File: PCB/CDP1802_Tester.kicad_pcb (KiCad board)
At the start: 2 copper layers, 102.2 x 53.8 mm, 7 parts, among them SW1 SW_Push, SW2 SW_Push, SW3 SW_Push, SW4 SW_Push, SW5 SW_Push, U1 CDP1802ACE

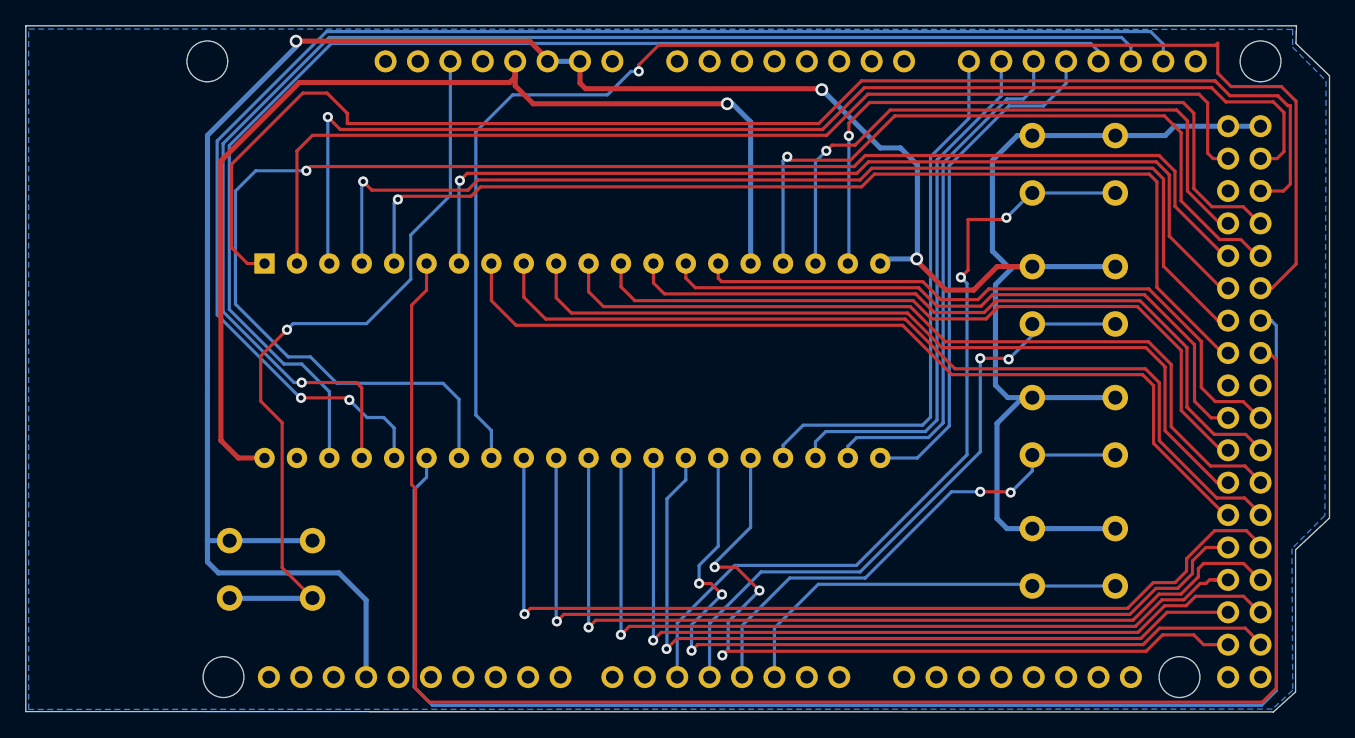
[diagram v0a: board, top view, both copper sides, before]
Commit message: Changed ZIF socket to wide (oval) pins Added jumper for pin 16 to either Vcc or A15 on the Arduino Added Reset button Set A15/PIN16 to OUTPUT and default HIGH Updated code to use SW3 to toggle the value of A15/PIN16
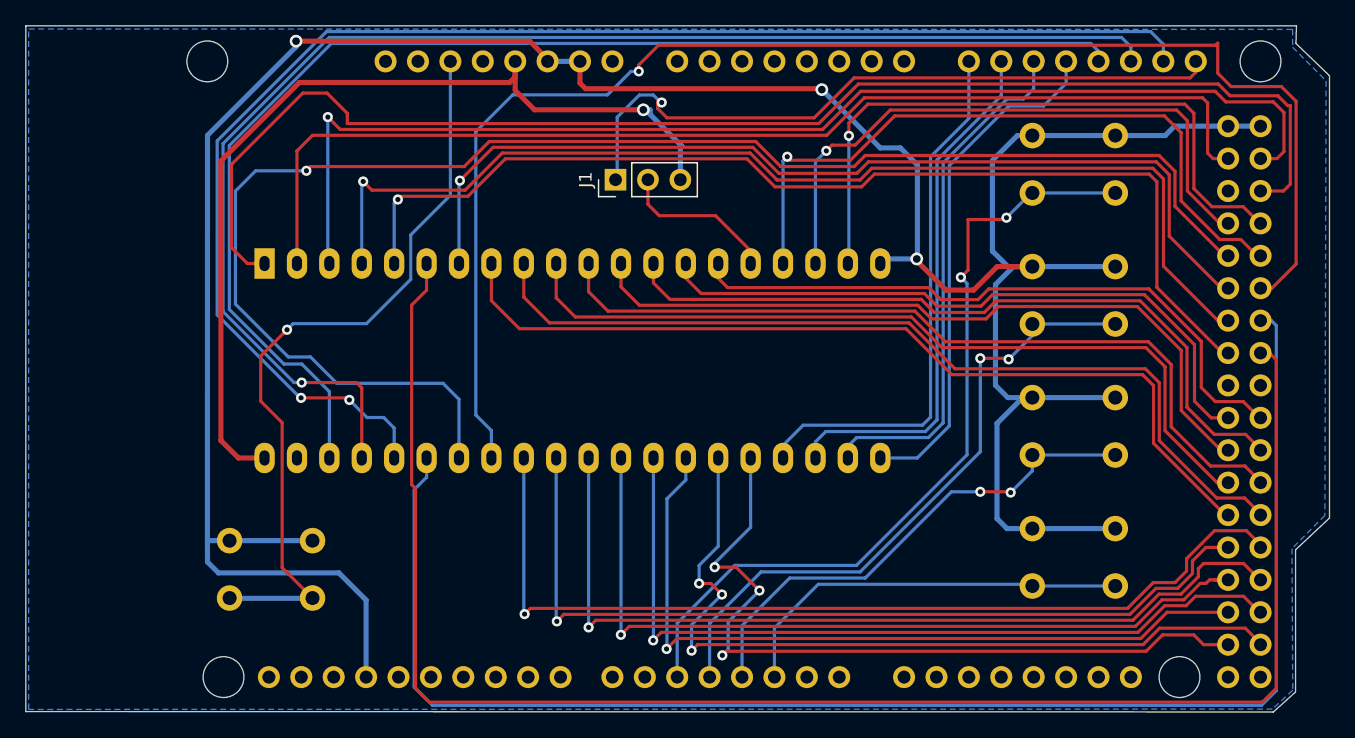
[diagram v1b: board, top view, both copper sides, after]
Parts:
- added J1: Conn_01x03, Pin_Headers:Pin_Header_Straight_1x03_Pitch2.54mm, F.Cu at (141.5, 29.6)
- U1: footprint Housings_DIP:DIP-40_W15.24mm -> ArduinoMega:DIP-40_W15.24mm_Socket_ZIF
- XA1: footprint Arduinos:Arduino_Mega2560_Shield_alt1 -> ArduinoMega:Arduino_Mega2560_Shield_alt1
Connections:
- U1 pad 16: VCC -> Net-(J1-Pad2)
- XA1 pad A15: (no net) -> Net-(J1-Pad1)
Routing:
- net Net-(J1-Pad1): track 0.00 -> 55.1 mm, vias 0 -> 1
- net VCC: track 85.7 -> 73.1 mm
- net Net-(J1-Pad2): track 0.00 -> 12.5 mm
- net /SC1: track 81.7 -> 83.5 mm
- net /Q: track 84.2 -> 86.0 mm
- net /MRD: track 74.3 -> 76.0 mm
- net /TPA: track 117.9 -> 119.5 mm
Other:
- board text added: "GPIO A15 (1804, 1805)"
- board text added: "Pin 16"
- board text added: "Vcc (1802, 1806)"
